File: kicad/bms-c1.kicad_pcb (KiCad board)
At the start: 4 copper layers, 135 x 70 mm, 207 parts, among them J1 MicroFit 2x12, J2 B4B-PH-SM4, J3 USB_B_Micro, J4 B3B-PH-SM4, J5 B2B-PH-SM4, J6 B4B-PH-SM4, P1 CONN_01X01, P2 CONN_01X01, P3 CONN_01X01, P4 CONN_01X01, P5 CONN_01X01, Q1 DMN10H220LE, Q10 BSS84, Q11 BSS123N, Q12 ZXMP10A17GTA, Q2 IPT015N10N5, Q3 IPT015N10N5, Q4 IPT015N10N5, Q5 IPT015N10N5, Q6 IPT015N10N5, Q7 IPT015N10N5, Q8 IPT015N10N5, Q9 IPT015N10N5, U1 SN65HVD230, U2 LMR16030, U4 BQ76952, U5 ESP32-C3-MINI-1

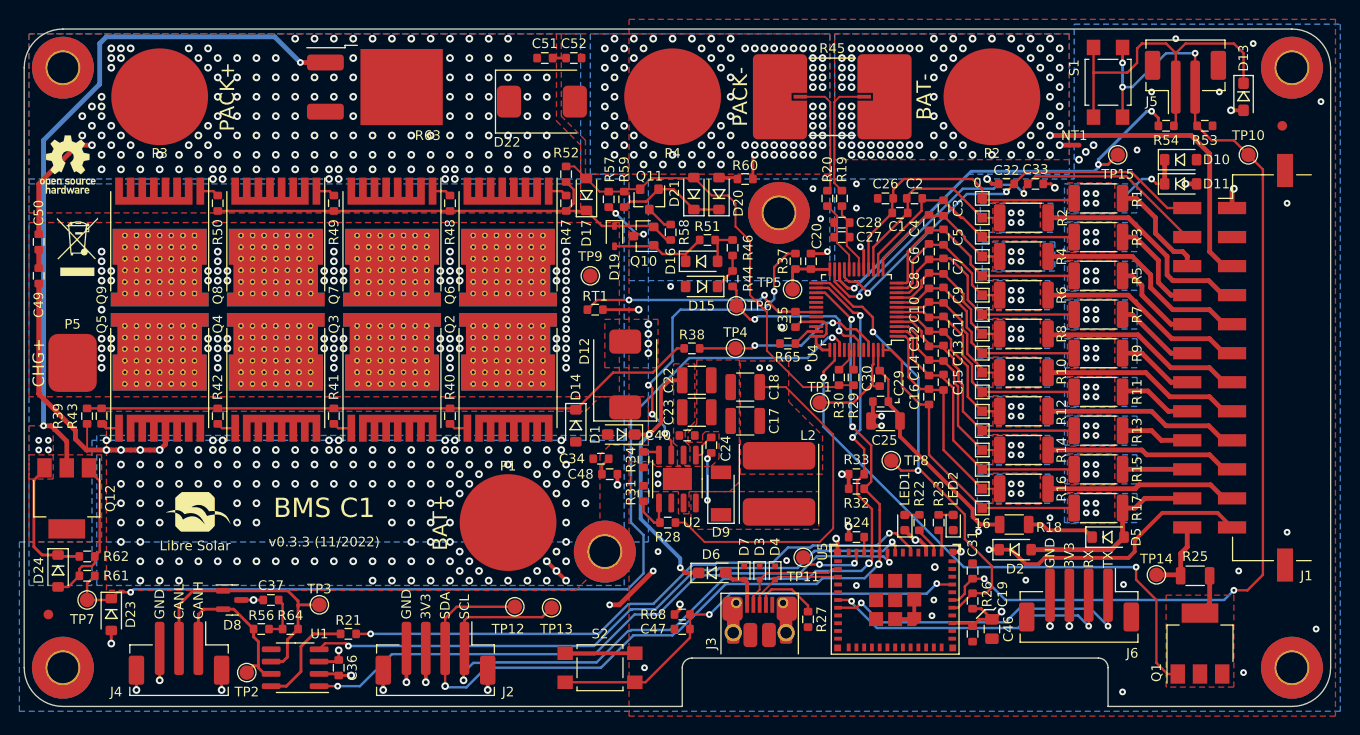
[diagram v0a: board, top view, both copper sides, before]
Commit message: v0.4.0: Multiple improvements for new board revision
- Use LMR38010 for internal power supply (max. 80V instead of 60V)
- Change USB connector from Micro-A to C and remove 5V power supply
  which was not working anyway. The board cannot be powered by USB
  only.
- Add TS2 (connected to DFETOFF) to measure shunt temperature
- Add RS-485 transceiver (sharing the connector with CAN)
- Switch I2C pins of ESP32-C3 to GPIO8/9. This allows to re-use the
  I2C pull-ups for strapping configuration and frees two pins for the
  RS-485 transceiver RE and DE pins. Also we may get rid of the I2C
  glitches during start-up.
- Reduce DSG gate resistor R57 to 47R to increase switch-off speed.
- Use more easily available and cheaper Würth 7466005R terminals with
  countersunk hole/thread.
- Adjust some resistors to reduce number of different parts
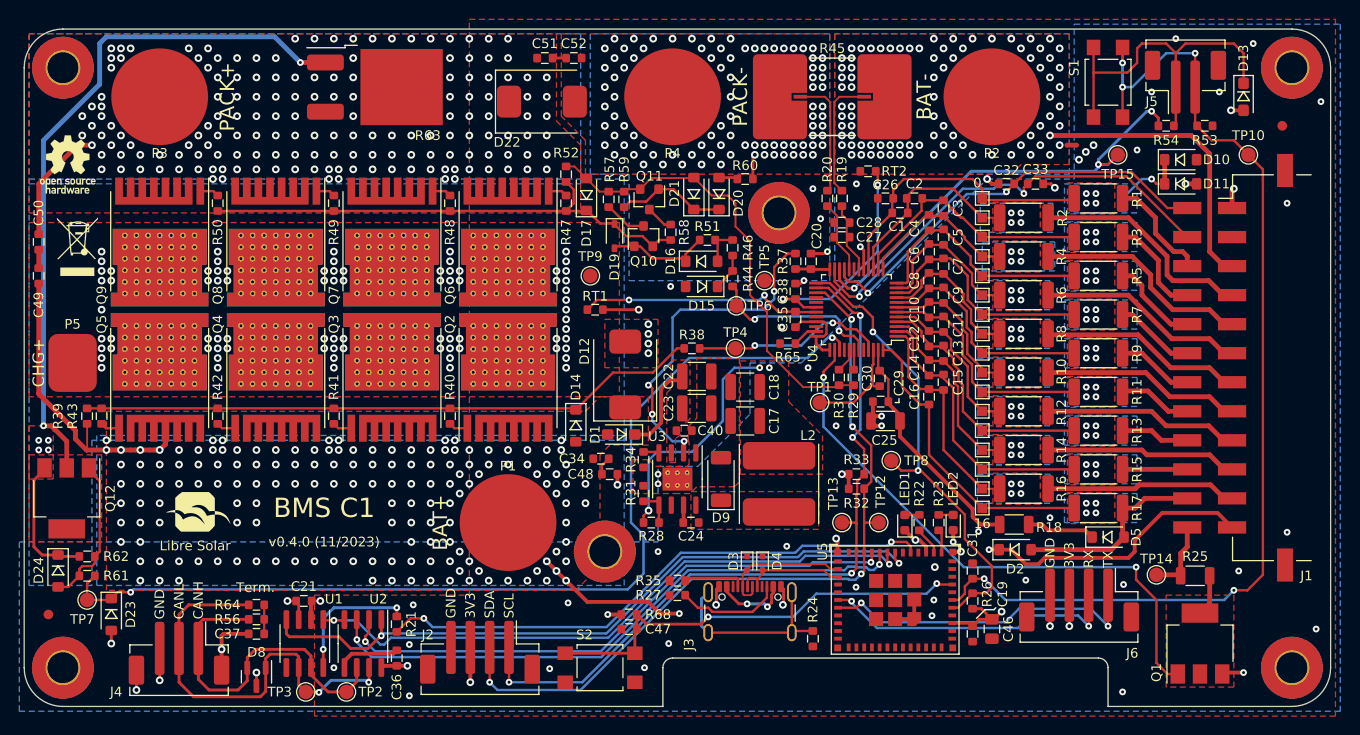
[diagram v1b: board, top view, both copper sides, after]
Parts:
- removed D6: PMEG10010ELRX, LibreSolar:D_SOD-123F
- removed D7: ESD5B5.0ST1G, LibreSolar:D_SOD-523
- removed TP11: TestPoint, TestPoint:TestPoint_Pad_D1.5mm
- added C21: 100nF, LibreSolar:C_0603_1608, F.Cu at (108.9, 109.1)
- added C38: 100pF, LibreSolar:C_0603_1608, F.Cu at (159.7, 77.1)
- added R35: 5.1k, LibreSolar:R_0603_1608, F.Cu at (147.5, 107.0)
- added RT2: 10k, LibreSolar:R_0603_1608, F.Cu at (167.2, 64.7)
- added U3: LMR38020, LibreSolar:SOIC-8-1EP_3.9x4.9mm_P1.27mm_EP2.4x3.1mm_ThermalVias, F.Cu at (147.5, 96.5)
- J3: value USB_B_Micro -> USB_C_Receptacle_USB2.0; footprint LibreSolar:USB_Micro-B_10103594-0001LF -> Connector_USB:USB_C_Receptacle_GCT_USB4105-xx-A_16P_TopMnt_Horizontal
- L2: value 10µH -> 22µH
- P1, P2, P3, P4: footprint LibreSolar:Wuerth_PowerOne_SMD_LF990005 -> LibreSolar:Wuerth_WP-SMBU_7466005R
- R24: value 10k -> 1M
- R27: value 330k -> 5.1k
- R28, R65: value 100k -> 82k
- R31: value 29.4k -> 35.7k
- R34: value 49.9k -> 52.3
- R53: value 6.8k -> 5.1k
- R54: value 4.7k -> 5.1k
- U2: value LMR16030 -> SN65HVD75; footprint Package_SO:SOIC-8-1EP_3.9x4.9mm_P1.27mm_EP2.29x3mm -> Package_SO:SOIC-8_3.9x4.9mm_P1.27mm
- moved TP12 38.6 mm to (168.3, 101.0)
- moved U2 36.7 mm to (115.0, 113.5)
- moved TP13 31.3 mm to (164.5, 101.0)
- moved R27 13.7 mm to (147.5, 108.5), turned to 0 degrees
- moved R24 11.4 mm to (161.5, 113.0), turned to 90 degrees
- moved TP2 10.5 mm to (113.3, 118.5)
- moved TP3 9.11 mm to (109.1, 118.5)
- moved D8 8.32 mm to (104.0, 116.9), turned to -90 degrees
- moved C24 8.27 mm to (148.9, 101.0), turned to 0 degrees
- moved C36 6.08 mm to (118.5, 115.0), turned to 90 degrees
- moved C47 5.50 mm to (142.5, 112.0)
- moved R68 5.50 mm to (142.5, 110.5)
- moved R21 5.10 mm to (118.5, 111.5), turned to -90 degrees
- moved J2 4.60 mm to (127.1, 114.4)
- moved R64 4.30 mm to (104.0, 109.5), turned to 180 degrees
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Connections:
- C24 pad 1: Net-(C24-Pad1) -> Net-(U3-BOOT)
- R24 pad 1: Net-(R24-Pad1) -> GND
- R24 pad 2: +3V3 -> Net-(J3-SHIELD)
- R27 pad 1: Net-(J3-Pad4) -> GND
- R27 pad 2: GND -> Net-(J3-CC2)
- R34 pad 1: Net-(R34-Pad1) -> Net-(U3-RT/SYNC)
- TP5 pad 1: /REG18 -> /Power Supply/EN
- U2 pad 1: Net-(C24-Pad1) -> /ESP32-C3 MCU/CAN_RX
- U2 pad 2: /Power Supply/VIN -> /ESP32-C3 MCU/RS485_~{RE}
- U2 pad 3: /Power Supply/EN -> /ESP32-C3 MCU/RS485_DE
- U2 pad 4: Net-(R34-Pad1) -> /ESP32-C3 MCU/CAN_TX
- U2 pad 5: /Power Supply/FB -> GND
- U2 pad 6: unconnected-(U2-Pad6) -> /CAN_H
- U2 pad 7: GND -> /CAN_L
- U2 pad 8: /Power Supply/SW -> +3V3
- U4 pad 30: unconnected-(U4-Pad30) -> /BQ76952/TEMP_SHUNT
- U5 pad 20: /I2C_SDA -> /ESP32-C3 MCU/RS485_DE
- U5 pad 21: /I2C_SCL -> /ESP32-C3 MCU/RS485_~{RE}
- U5 pad 22: Net-(R24-Pad1) -> /I2C_SDA
- U5 pad 23: /ESP32-C3 MCU/BOOT -> /I2C_SCL
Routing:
- net /ESP32-C3 MCU/RS485_DE: track 0.00 -> 62.5 mm, vias 0 -> 2
- net /ESP32-C3 MCU/RS485_~{RE}: track 0.00 -> 60.0 mm, vias 0 -> 2
- net /BQ76952/TEMP_SHUNT: track 0.00 -> 24.0 mm, vias 0 -> 2
- net Net-(J3-SHIELD): track 0.00 -> 19.8 mm
- net /CAN_H: track 17.6 -> 35.9 mm
- net /Power Supply/VIN: track 27.2 -> 9.27 mm, vias 2 -> 0
- net /I2C_SCL: track 96.4 -> 79.1 mm
- net +3V3: track 137.7 -> 121.2 mm, vias 12 -> 11
- net /CAN_L: track 28.4 -> 44.1 mm, vias 0 -> 2
- net /I2C_SDA: track 96.8 -> 81.4 mm
- net Net-(J3-CC2): track 0.00 -> 10.9 mm
- net unconnected-(J3-VBUS-PadA4): track 0.00 -> 7.70 mm, vias 0 -> 2
- net /ESP32-C3 MCU/CAN_RX: track 65.3 -> 72.9 mm
- net Net-(J3-Pad4): track 6.93 -> 0.00 mm
- net /ESP32-C3 MCU/BOOT: track 6.90 -> 0.00 mm, vias 2 -> 0
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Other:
- outline, holes or cut-outs redrawn
- board text added: "4-layer PCB 70µm outer layers 70µm inner layers Silkscreen top only"
- board text added: "Term."
- board text added: "v0.4.0 (11/2023)"
- board text removed: "4-layer PCB 105µm outer layers 70µm inner layers Silkscreen top only"
- board text removed: "v0.3.3 (11/2022)"
